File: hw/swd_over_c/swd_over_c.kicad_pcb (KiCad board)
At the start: 4 copper layers, 27 x 13 mm, 17 parts, among them J1 USB_C_Receptacle, J2 Conn_ARM_JTAG_SWD_10, J3 USB_C_Receptacle, U1 ATtiny24-20M

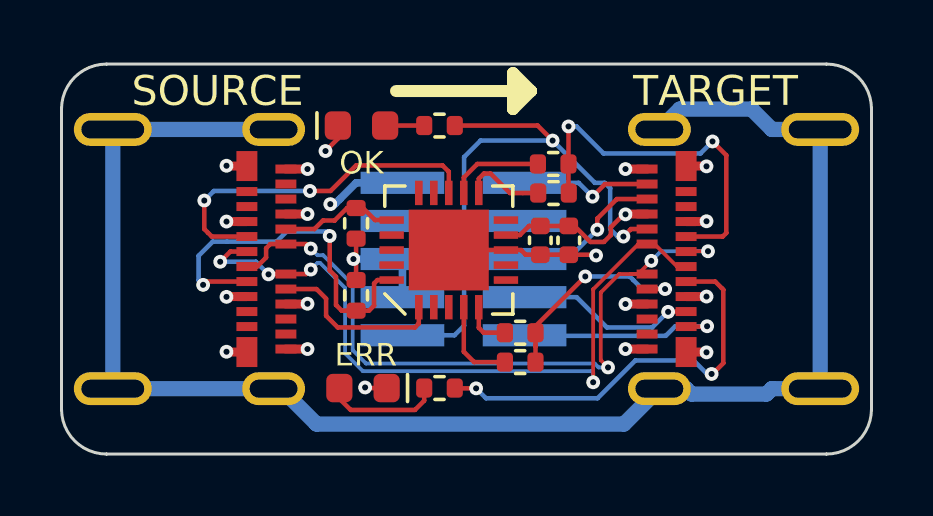
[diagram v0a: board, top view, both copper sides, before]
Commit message: v3.0 SWD2USBC
Had the tx/rx pairs flipped since I switched from USB-C Plug to Connector...
Removed MCU since cables don't connect both CC1/CC2 so can't actually do a proper debug accessory mode.
Should still work though?
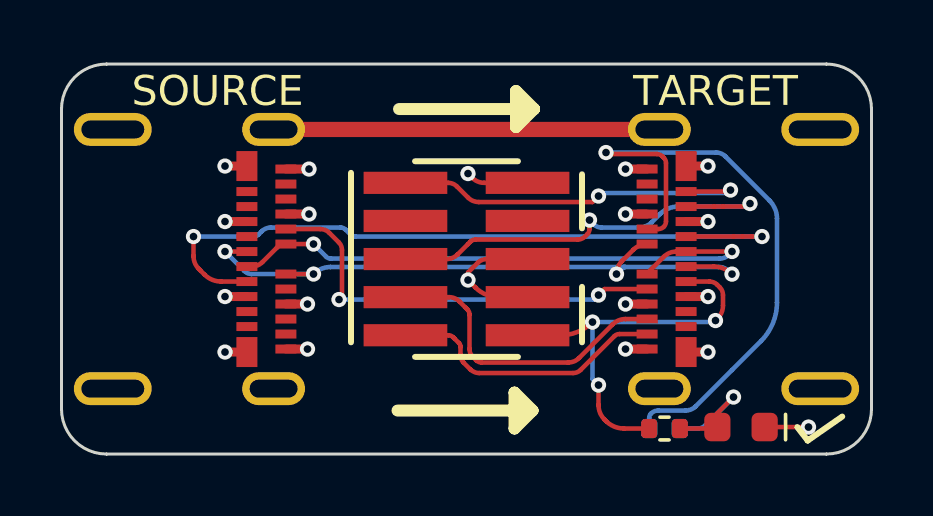
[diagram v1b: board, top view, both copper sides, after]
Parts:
- removed C1: 1uF, Capacitor_SMD:C_0402_1005Metric
- removed C2: 0.1uF, Capacitor_SMD:C_0402_1005Metric
- removed D2: RED, LED_SMD:LED_0603_1608Metric
- removed R3, R6: 22k, Resistor_SMD:R_0402_1005Metric
- removed R4: 10k, Resistor_SMD:R_0402_1005Metric
- removed R5: 56k, Resistor_SMD:R_0402_1005Metric
- removed R7, R8: 1k, Resistor_SMD:R_0402_1005Metric
- removed U1: ATtiny24-20M, ultralibrarian:ATTINY24A-MU
- J2: moved to F.Cu
- R1: value 5.1k -> 1k
- R2: value 5.1k -> DNP; moved to B.Cu
- moved D1 16.2 mm to (177.7, 105.6), turned to 180 degrees
- moved R2 12.3 mm to (175.1, 105.7), turned to 0 degrees
- moved R1 11.2 mm to (175.1, 105.7), turned to 0 degrees
- moved REF** 8.20 mm to (168.4, 100.2), turned to 0 degrees
- moved J2 0.10 mm to (168.5, 100.0)
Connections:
- J1 pad A5: /CC1_IN_MOSI -> /CC1
- J1 pad B5: /CC2_IN_MISO -> /CC2
- J2 pad 1: /SBU1 -> /SBU2
- J3 pad A10: /SWO -> unconnected-(J3-PadA10)
- J3 pad A11: /NRST -> unconnected-(J3-PadA11)
- J3 pad A2: unconnected-(J3-PadA2) -> /SWDIO
- J3 pad A3: unconnected-(J3-PadA3) -> /SWDCLK
- J3 pad B10: /SWDCLK -> unconnected-(J3-PadB10)
- J3 pad B11: /SWDIO -> unconnected-(J3-PadB11)
- J3 pad B2: unconnected-(J3-PadB2) -> /NRST
- J3 pad B3: unconnected-(J3-PadB3) -> /SWO
- R1 pad 1: GND -> /SBU2
- R1 pad 2: /CC2_IN_MISO -> Net-(D1-Pad2)
- R2 pad 1: GND -> /SBU1
- R2 pad 2: /CC1_IN_MOSI -> Net-(D1-Pad2)
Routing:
- net /SHIELD: track 53.3 -> 12.9 mm
- net /CC2_IN_MISO: track 12.5 -> 0.00 mm, vias 2 -> 0
- net /CC2: track 12.2 -> 24.5 mm
- net /MCURST: track 11.9 -> 0.00 mm, vias 2 -> 0
- net /SWO: track 5.13 -> 14.7 mm, vias 1 -> 2
- net /NRST: track 4.45 -> 12.7 mm, vias 1 -> 2
- net /CC1: track 6.99 -> 14.3 mm
- net /SCK: track 5.89 -> 0.00 mm
- net GND: track 19.4 -> 14.0 mm, vias 13 -> 11
- net VBUS: track 10.5 -> 5.85 mm
- net /SWDCLK: track 6.01 -> 10.3 mm, vias 1 -> 0
- net /CC1_IN_MOSI: track 3.98 -> 0.00 mm
- net Net-(D2-Pad2): track 3.88 -> 0.00 mm
- net /D+: track 23.5 -> 19.8 mm, vias 4 -> 2
- net Net-(D1-Pad2): track 1.30 -> 4.70 mm, vias 0 -> 1
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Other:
- board text added: "alvarop.com"
- board text added: "v3.0"
- board text removed: "ERR"
- board text removed: "OK"
- board text removed: "by @alvaroprieto"
- board text removed: "v2.0"

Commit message: Release SWD over C v4.0
Swapped Tx/Rx lines since USB C cables cross them over...
Thanks to Matthias for reporting the bug!
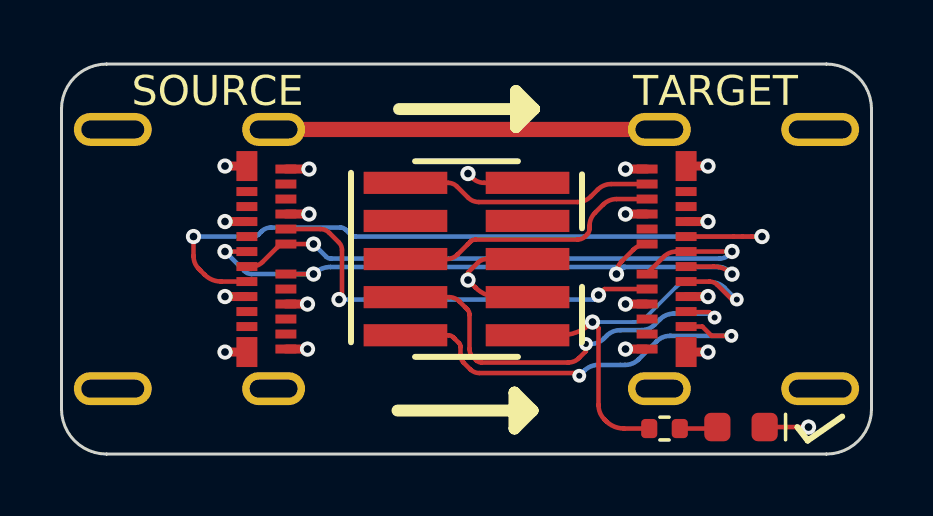
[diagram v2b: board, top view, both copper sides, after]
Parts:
- removed R2: DNP, Resistor_SMD:R_0402_1005Metric
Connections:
- J1 pad A8: /SCK -> unconnected-(J1-PadA8)
- J1 pad B8: /MCURST -> unconnected-(J1-PadB8)
- J3 pad A10: unconnected-(J3-PadA10) -> /SWO
- J3 pad A11: unconnected-(J3-PadA11) -> /NRST
- J3 pad A2: /SWDIO -> unconnected-(J3-PadA2)
- J3 pad A3: /SWDCLK -> unconnected-(J3-PadA3)
- J3 pad A8: /SBU1 -> unconnected-(J3-PadA8)
- J3 pad B10: unconnected-(J3-PadB10) -> /SWDCLK
- J3 pad B11: unconnected-(J3-PadB11) -> /SWDIO
- J3 pad B2: /NRST -> unconnected-(J3-PadB2)
- J3 pad B3: /SWO -> unconnected-(J3-PadB3)
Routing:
- net /SBU1: track 21.0 -> 0.00 mm, vias 1 -> 0
- net /SWO: track 14.7 -> 9.03 mm, vias 2 -> 0
- net /SWDIO: track 9.32 -> 13.8 mm, vias 0 -> 2
- net /NRST: track 12.7 -> 8.46 mm, vias 2 -> 0
- net /SWDCLK: track 10.3 -> 13.7 mm, vias 0 -> 2
- net Net-(D1-Pad2): track 4.70 -> 1.27 mm, vias 1 -> 0
- net /SBU2: track 13.7 -> 14.7 mm, vias 3 -> 2
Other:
- board text added: "v4.0"
- board text removed: "v3.0"
